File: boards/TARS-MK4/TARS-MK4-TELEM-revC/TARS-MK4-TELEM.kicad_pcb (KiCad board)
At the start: 2 copper layers, 86 x 79.1 mm, 83 parts, among them J101 U.FL, J102 B404X, J103 USB_B_Micro, J104 U.FL, J105 Conn_01x04, J106 Conn_01x02, J107 USB_B_Micro, J108 Molex_SlimStack_2091680401_2x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, J109 Molex_SlimStack_2091680401_2x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, J110 Conn_01x02, J111 Conn_01x04, J112 Molex_SlimStack_Plug_2x20_P0.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, J113 Molex_SlimStack_Plug_2x20_P0.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, J114 Conn_01x03, J115 Conn_01x02, J116 Conn_01x05, SW101 SW_Push, SW102 SW_Push, SW103 SW_Push, SW104 SW_Push, U101 MAX-M10S, U102 RFM96W-433S2, U103 USBLC6-2P6, U104 ESP32-S3-WROOM-1U, U105 TI_TPS564247DRLR, U106 USBLC6-2P6

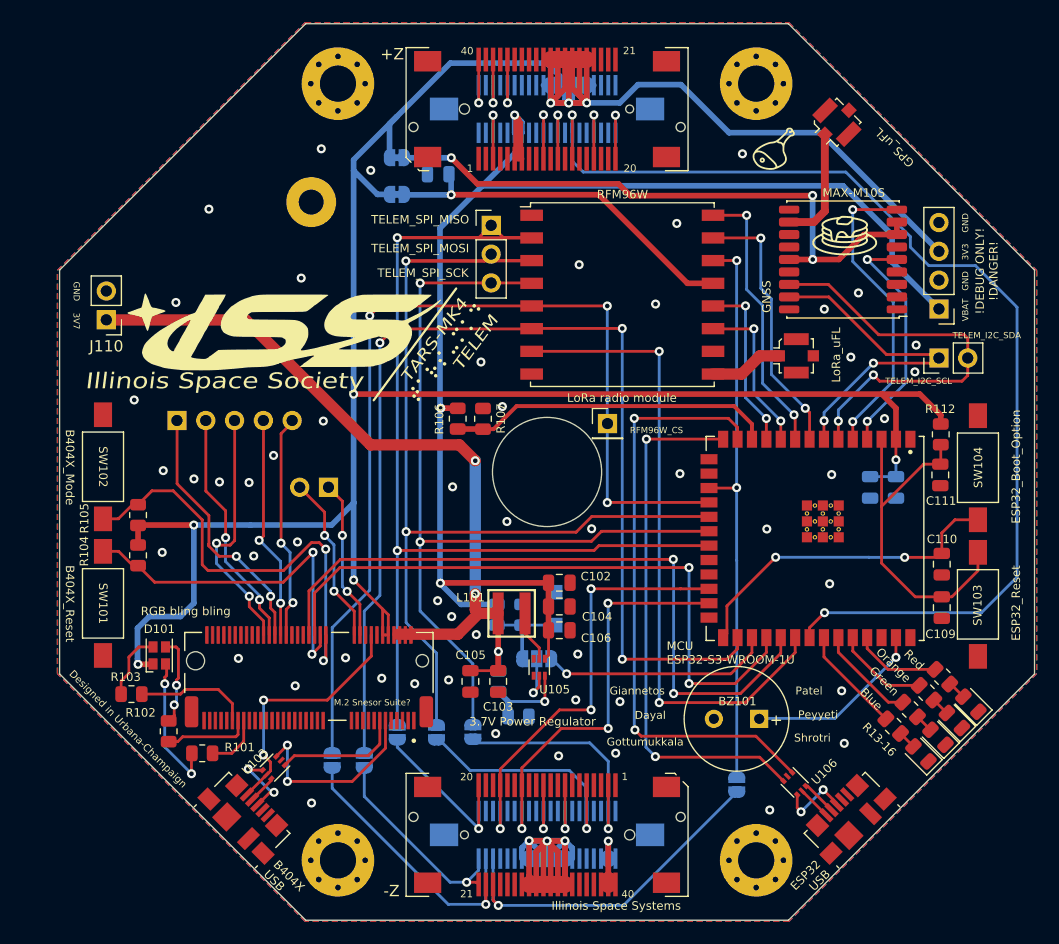
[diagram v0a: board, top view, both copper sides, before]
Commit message: Make Rev.C with mounting pin on BTB's, fixed some reference matching
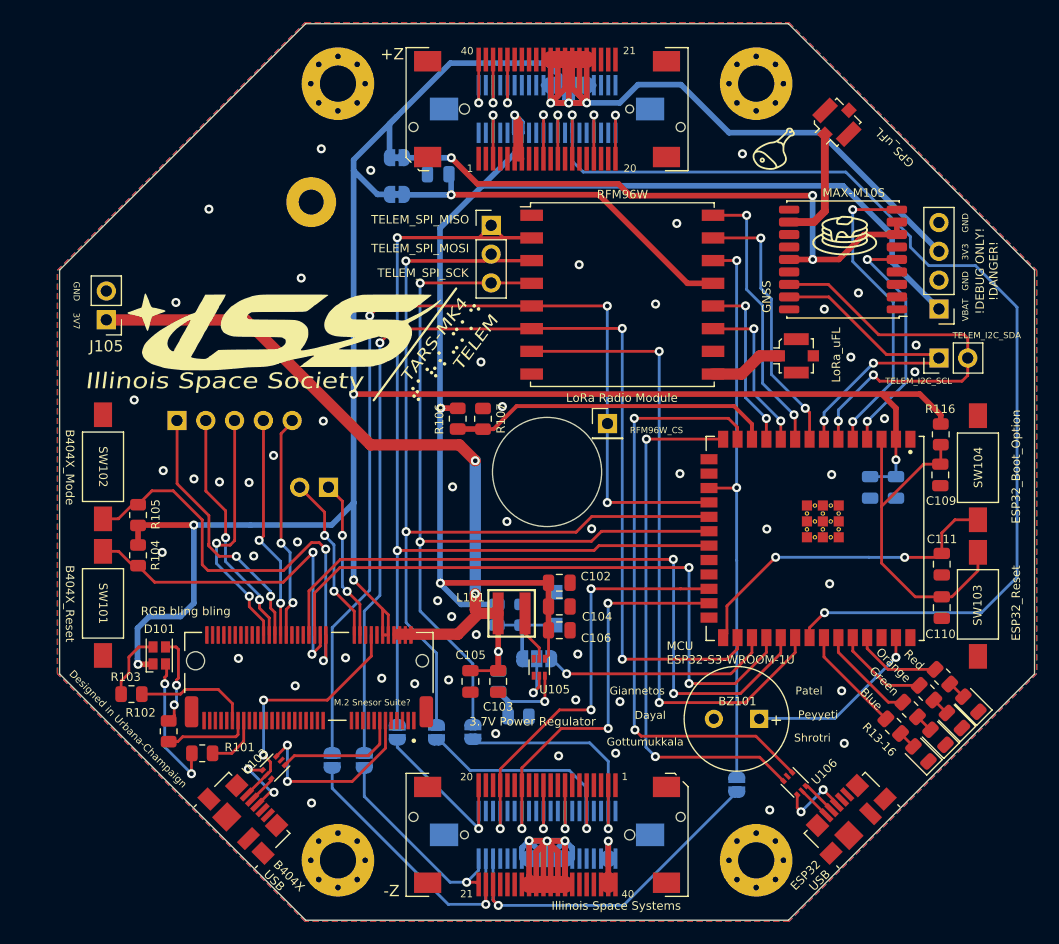
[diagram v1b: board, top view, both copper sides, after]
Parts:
- J110: renamed from J108; footprint Connector_Molex_BTB:Molex_SlimStack_2091680401_2x20_P0.635mm -> Connector_Molex_BTB:Molex_SlimStack_Receptacle_2091680401_2x20_P0.635mm
- J111: renamed from J109; footprint Connector_Molex_BTB:Molex_SlimStack_2091680401_2x20_P0.635mm -> Connector_Molex_BTB:Molex_SlimStack_Receptacle_2091680401_2x20_P0.635mm
- J115: renamed from J112; footprint Connector_Molex_BTB:Molex_SlimStack_Plug_2x20_P0.365mm -> Connector_Molex_BTB:Molex_SlimStack_Plug_550910474_2x20_P0.365mm
- J116: renamed from J113; footprint Connector_Molex_BTB:Molex_SlimStack_Plug_2x20_P0.365mm -> Connector_Molex_BTB:Molex_SlimStack_Plug_550910474_2x20_P0.365mm
- renumbered C111 to C109, C109 to C110, C110 to C111, J110 to J105, J111 to J106, J105 to J107, J106 to J108, J107 to J109, J114 to J112, J115 to J113, J116 to J114, R113 to R112, R114 to R113, R115 to R114, R116 to R115, R112 to R116
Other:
- board text added: "LoRa Radio Module"
- board text removed: "LoRa radio module"

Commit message: Added ESD chips and RTL-SDR pins
Added ESD chips and RTL-SDR pins
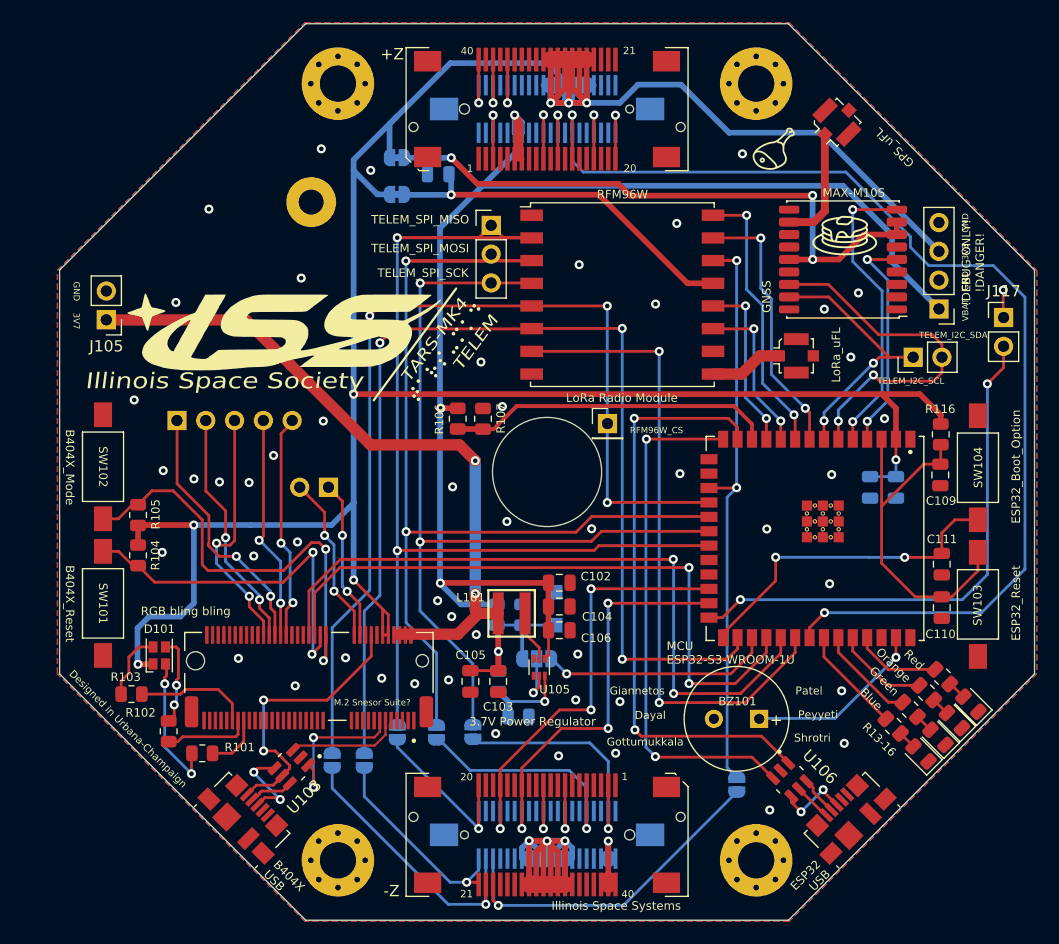
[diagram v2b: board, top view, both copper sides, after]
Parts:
- added J117: Conn_01x02, Connector_PinHeader_2.54mm:PinHeader_1x02_P2.54mm_Vertical, F.Cu at (140.3, 86.4)
- J115, J116: value Molex_SlimStack_Plug_2x20_P0.365mm -> Molex_SlimStack_Plug_550910474_2x20_P0.365mm
- U103, U106: footprint Package_TO_SOT_SMD:SOT-666 -> SOT95P280X145-6N:SOT95P280X145-6N
- moved J113 2.28 mm to (132.3, 89.9)
- moved U103 1.56 mm to (77.5, 126.0)
- moved U106 0.55 mm to (121.4, 127.1)
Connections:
- U104 pad 26: unconnected-(U104-Pad26) -> /RTL_SDR_EN
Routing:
- net /RTL_SDR_EN: track 0.00 -> 46.8 mm, vias 0 -> 2
- net /LTE_USB_DP: track 16.9 -> 9.96 mm, vias 2 -> 0
- net /TELEM_I2C_SCL: track 29.9 -> 23.3 mm
- net /TELEM_I2C_SDA: track 36.7 -> 31.7 mm
- net /LTE_USB_5V: track 22.4 -> 25.7 mm
- net GND: track 0.00 -> 2.44 mm, vias 53 -> 51
- net /LTE_USB_DN: track 11.2 -> 13.6 mm, vias 0 -> 2
- net /TEENSY_SWITCH: track 99.5 -> 101.0 mm
- net Net-(J103-Pad2): track 2.54 -> 3.96 mm
- net Net-(J103-Pad3): track 6.35 -> 7.70 mm
- net /MAX-M10S_INT: track 21.3 -> 20.0 mm
- net /ESP_USB_DP: track 47.3 -> 46.3 mm
- net /MAX-M10S_RESET: track 27.1 -> 26.3 mm
- net /TELEM_INT: track 50.1 -> 50.8 mm
- net /ESP_USB_DN: track 53.4 -> 52.7 mm

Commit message: Removed bad commit
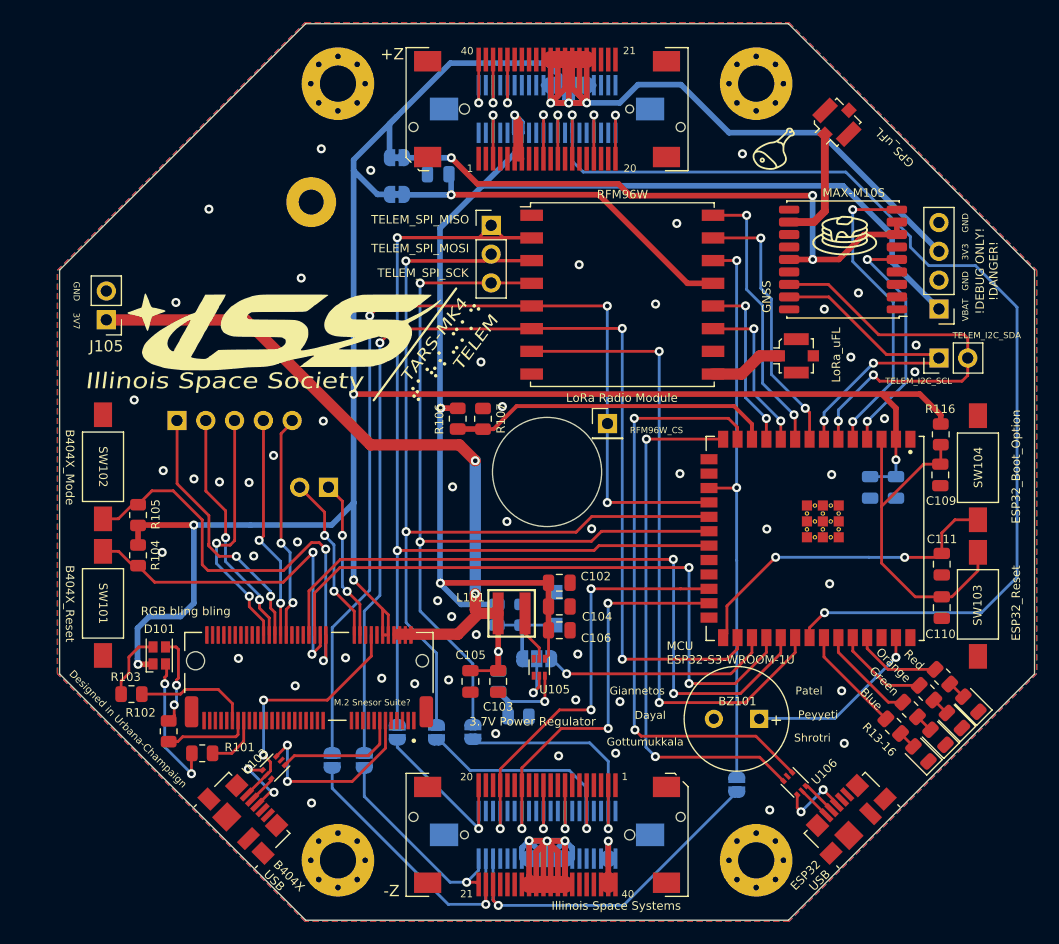
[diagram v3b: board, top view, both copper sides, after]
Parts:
- removed J117: Conn_01x02, Connector_PinHeader_2.54mm:PinHeader_1x02_P2.54mm_Vertical
- J115, J116: value Molex_SlimStack_Plug_550910474_2x20_P0.365mm -> Molex_SlimStack_Plug_2x20_P0.365mm
- U103, U106: footprint SOT95P280X145-6N:SOT95P280X145-6N -> Package_TO_SOT_SMD:SOT-666
- moved J113 2.28 mm to (134.6, 90.0)
- moved U103 1.56 mm to (75.9, 126.1)
- moved U106 0.55 mm to (121.8, 127.5)
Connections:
- U104 pad 26: /RTL_SDR_EN -> unconnected-(U104-Pad26)
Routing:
- net /RTL_SDR_EN: track 46.8 -> 0.00 mm, vias 2 -> 0
- net /LTE_USB_DP: track 9.96 -> 16.9 mm, vias 0 -> 2
- net /TELEM_I2C_SCL: track 23.3 -> 29.9 mm
- net /TELEM_I2C_SDA: track 31.7 -> 36.7 mm
- net /LTE_USB_5V: track 25.7 -> 22.4 mm
- net GND: track 2.44 -> 0.00 mm, vias 51 -> 53
- net /LTE_USB_DN: track 13.6 -> 11.2 mm, vias 2 -> 0
- net /TEENSY_SWITCH: track 101.0 -> 99.5 mm
- net Net-(J103-Pad2): track 3.96 -> 2.54 mm
- net Net-(J103-Pad3): track 7.70 -> 6.35 mm
- net /MAX-M10S_INT: track 20.0 -> 21.3 mm
- net /ESP_USB_DP: track 46.3 -> 47.3 mm
- net /MAX-M10S_RESET: track 26.3 -> 27.1 mm
- net /TELEM_INT: track 50.8 -> 50.1 mm
- net /ESP_USB_DN: track 52.7 -> 53.4 mm
